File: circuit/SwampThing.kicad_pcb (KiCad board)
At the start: 2 copper layers, 102 parts, among them J1 USB_B, J2 HOLE, J3 HOLE, J4 HOLE, J5 HOLE, Q1 IRF530NPbF, Q2 BC547, SW1 reset, SW2 mute, SW3 HEAD/AD, SW4 vol+, SW5 vol-, SW6 next, SW7 prev, SW8 pause, U1 LM2576T-ADJ, U2 LM1117-5.0, U3 MAX6457, U4 LM1117-3.3, U5 TPA3220, U6 CSR_DBG, U7 CSR8645_MODULE

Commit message: SwampThing routed!
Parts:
- removed C13, C31: 470μF, NovaBox:CPOL_D10_P4.5
- removed C20: 10μF, NovaBox:CPOL_D6.3_P2.5
- removed C39: 1μF, NovaBox:CPOL_D4_P2
- removed S1: BATT_SEL, NovaBox:BATT_SEL
- removed SW4: vol+, NovaBox:Tact_6x6
- removed SW5: vol-, NovaBox:Tact_6x6
- removed SW7: prev, NovaBox:Tact_6x6
- added C6: 860μF, NovaBox:CPOL_D16_P7.5, F.Cu at (102.2, 80.6)
- added SW10: 4S LiPo, NovaBox:Switch_2.5mm, F.Cu at (77.9, 108.4)
- added SW11: 3S LiPo, NovaBox:Switch_2.5mm, F.Cu at (77.9, 105.9)
- added SW9: 6S LiPo, NovaBox:Switch_2.5mm, F.Cu at (77.9, 111.0)
- BT1: footprint NovaBox:XT60-M -> NovaBox:XT60PW-M
- C17, C19, C23, C24, C27, C34, C35: footprint NovaBox:C_5MM -> NovaBox:C_1206
- C38, C41: footprint NovaBox:CPOL_D4_P2 -> NovaBox:CPOL_D4_P1.27
- C4: value 100μF -> 860μF; footprint NovaBox:CPOL_D6.3_P2.5 -> NovaBox:CPOL_D16_P7.5
- C8: footprint NovaBox:CPOL_D10_P4.5 -> NovaBox:CPOL_D6.3_P2.5
- D5: value LED_RCBG -> LED_RABG; footprint NovaBox:LED_RCBG -> NovaBox:LED_RABG
- Q1: value IRF530NPbF -> IRF530NSPbF; footprint NovaBox:TO-220_Horizontal -> NovaBox:TO-252
- R11: value 1K -> 10K
- R24: value 470 -> 820
- R26: value 470 -> 220
- R27: value 470 -> 1K
- S2: value JUMPER_3WAY -> 18dB
- S3: value JUMPER_3WAY -> 24dB
- S4: value JUMPER_3WAY -> 30dB
- S5: value JUMPER_3WAY -> 34dB
- SW1, SW2: footprint NovaBox:Tact_6x6 -> NovaBox:Switch_2.5mm
- U1: footprint NovaBox:TO-220-5_Horizontal -> NovaBox:TO-263-5_TabPin3
- moved SW6 142.4 mm to (57.8, 52.1), turned to 90 degrees
- moved J1 127.1 mm to (47.6, 94.0), turned to 270 degrees
- moved J4 124.1 mm to (49.0, 34.0)
- moved C41 108.1 mm to (56.8, 95.9), turned to 270 degrees
- moved C5 107.2 mm to (130.8, 40.0)
- moved C10 106.5 mm to (105.4, 48.3)
- moved C12 106.0 mm to (102.3, 55.5)
- moved C15 106.0 mm to (130.8, 53.3)
- moved SPK1 105.9 mm to (140.4, 47.0)
- moved C11 105.6 mm to (105.4, 51.4)
- moved C29 105.6 mm to (105.4, 67.0)
- moved C30 105.6 mm to (106.1, 62.4)
- moved U5 105.6 mm to (96.0, 59.4)
- moved C22 105.6 mm to (106.1, 57.0)
- moved L2 105.6 mm to (118.1, 46.0)
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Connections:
- net +7V renamed +7.5V
- net Net-(C35-Pad1) renamed /GVDD
- net Net-(R20-Pad1) renamed /RESET
- C4 pad 1: +5V -> +BATT
- R11 pad 1: +5V -> +BATT
- R21 pad 1: Net-(R21-Pad1) -> GND
- R21 pad 2: GND -> /FREQ_ADJ
- R24 pad 2: Net-(D5-PadRA) -> Net-(D5-Pad1)
- R26 pad 2: Net-(D5-PadBA) -> Net-(D5-Pad3)
- R27 pad 2: Net-(D5-PadGA) -> Net-(D5-Pad4)
- U5 pad 14: Net-(R21-Pad1) -> /FREQ_ADJ
- U7 pad 30: /PREV -> (no net)
- U7 pad 32: /VOL- -> (no net)
- U7 pad 33: /VOL+ -> (no net)
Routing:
- net +BATT: track 0.00 -> 260.8 mm
- net +5V: track 0.00 -> 123.1 mm
- net GND: track 0.00 -> 85.6 mm, vias 0 -> 37
- net +7.5V: track 0.00 -> 58.7 mm, vias 0 -> 1
- net -BATT: track 0.00 -> 55.8 mm
- net +3V3: track 0.00 -> 55.3 mm, vias 0 -> 1
- net 1V8: track 0.00 -> 54.6 mm, vias 0 -> 1
- net Net-(S2-Pad2): track 0.00 -> 53.7 mm
- net VBUS: track 0.00 -> 47.5 mm, vias 0 -> 1
- net Net-(J1-Pad3): track 0.00 -> 43.6 mm, vias 0 -> 1
- net SPK_RP: track 0.00 -> 41.7 mm
- net Net-(J1-Pad2): track 0.00 -> 41.4 mm, vias 0 -> 1
- net SPK_RN: track 0.00 -> 41.0 mm
- net SPK_LP: track 0.00 -> 40.0 mm
- net SPK_LN: track 0.00 -> 39.4 mm
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- added copper zone on B.Cu, net GND
- added copper zone on F.Cu, net GND
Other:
- board outline added: 100 x 100 mm
- board text added: "AD"
- board text added: "HEAD"
- board text added: "SwampThing"

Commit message: PCB done
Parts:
- added REF**: OSHW-Symbol_44.5x40mm_SilkScreen, NovaBox:OSHW-Symbol_44.5x40mm_SilkScreen, B.Cu at (121.3, 58.4)
- added REF**: KiCad-Logo2_12mm_SilkScreen, NovaBox:KiCad-Logo2_12mm_SilkScreen, B.Cu at (125.7, 92.7)
- L1: footprint NovaBox:COIL_LHL10TB681K -> NovaBox:COILCRAFT_RFS1317
- moved D1 14.6 mm to (115.6, 106.0), turned to 180 degrees
- moved C2 5.68 mm to (102.9, 106.0), turned to 180 degrees
- moved R4 4.45 mm to (103.5, 116.2)
- moved R2 4.44 mm to (106.0, 116.2)
- moved L1 2.54 mm to (116.2, 116.2)
- moved SW2 1.80 mm to (88.9, 80.6), turned to 180 degrees
- moved R20 0.90 mm to (87.6, 53.3)
- moved BT1 0.63 mm to (47.6, 112.4)
- turned C21 to 0 degrees
- turned C6 to 180 degrees
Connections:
- J1 pad 5: Net-(J1-Pad5) -> (no net)
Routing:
- net +5V: track 123.1 -> 138.4 mm
- net Net-(R2-Pad2): track 20.8 -> 25.3 mm
- net Net-(D1-Pad1): track 26.4 -> 22.0 mm
- net +BATT: track 260.8 -> 257.6 mm
- net Net-(U6-Pad3): track 8.85 -> 11.1 mm
- net +3V3: track 55.3 -> 53.3 mm
- net +7.5V: track 58.7 -> 57.2 mm, vias 1 -> 0
- net HEAD: track 20.6 -> 19.2 mm
- net Net-(U6-Pad5): track 9.45 -> 10.5 mm
- net Net-(C38-Pad2): track 9.13 -> 9.83 mm
- net Net-(C19-Pad2): track 7.41 -> 8.05 mm
- net -BATT: track 55.8 -> 55.1 mm
- net Net-(U6-Pad7): track 10.6 -> 11.1 mm
- net Net-(R8-Pad1): track 12.3 -> 12.8 mm
- net /OUT2_M: track 26.4 -> 26.9 mm
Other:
- board text added: "Swamp thing"
- board text added: "by Ferenc Szili 2019.feb.24"
- board text added: "https://github.com/nodep/NovaBox"
- board text removed: "SwampThing"

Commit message: still have to check the electrolytics
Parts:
- C4, C6: value 860μF -> 1000μF
- R12, R17: value 470 -> 1K
- moved REF** 0.19 mm to (125.7, 92.9)
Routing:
- net /SW_GATE: track 27.0 -> 41.7 mm
- net -BATT: track 55.1 -> 57.1 mm
- net Net-(R10-Pad1): track 13.5 -> 12.7 mm
- net Net-(R8-Pad1): track 12.8 -> 12.1 mm
- net Net-(R9-Pad1): track 13.2 -> 12.7 mm

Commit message: i think this should be it
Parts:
- C1: footprint NovaBox:CPOL_D8_P3.5 -> NovaBox:CPOL_D10_P4.5
- C3: footprint NovaBox:CPOL_D6.3_P2.5 -> NovaBox:CPOL_D4_P1.5
- C38, C41: footprint NovaBox:CPOL_D4_P1.27 -> NovaBox:CPOL_D4_P1.5
- moved REF** 2.08 mm to (127.6, 92.1)
- moved C41 0.74 mm to (57.1, 96.5)
- moved C1 0.64 mm to (128.3, 104.1)
- moved D1 0.63 mm to (114.9, 106.0)
- moved C3 0.31 mm to (103.5, 94.6)
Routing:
- net VBUS: track 47.5 -> 48.1 mm

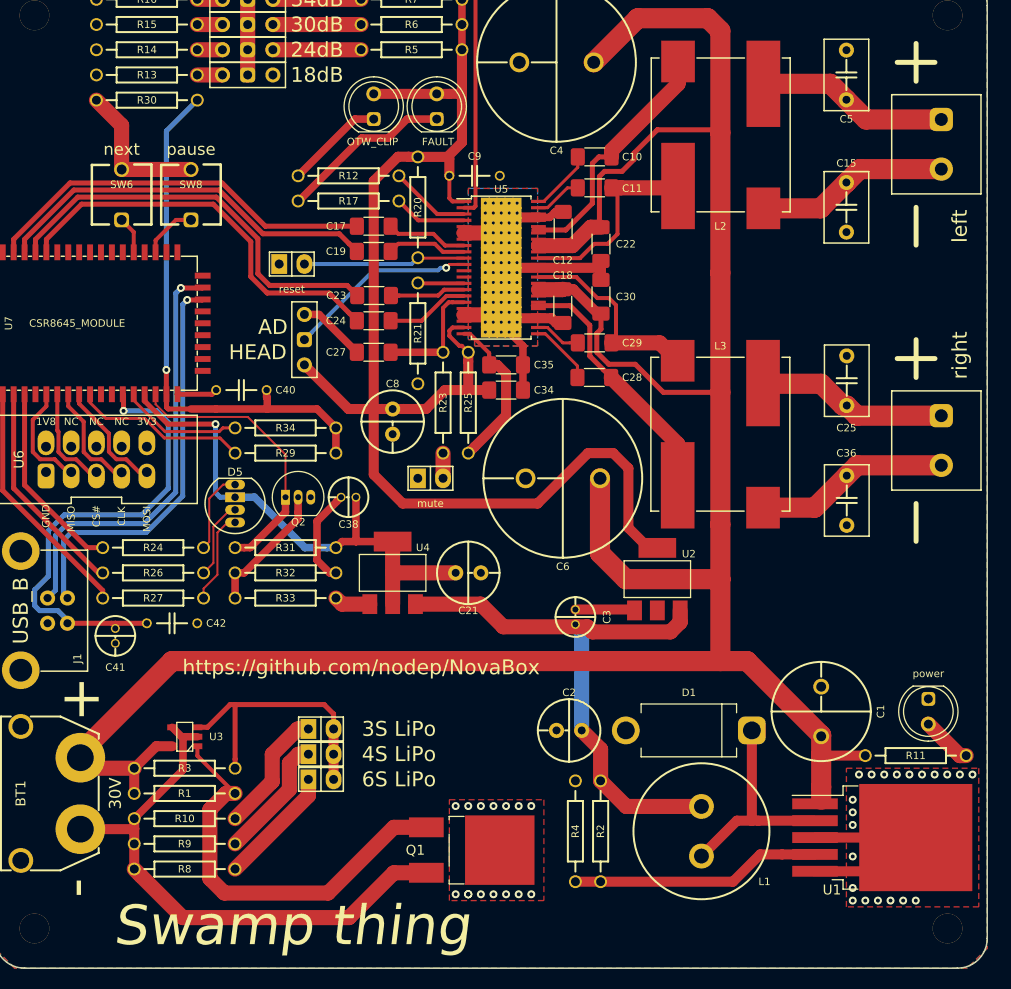
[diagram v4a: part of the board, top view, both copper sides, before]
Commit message: sent swamp thing to the fab fixed problem with voltages above 16V on the WhiteBoy
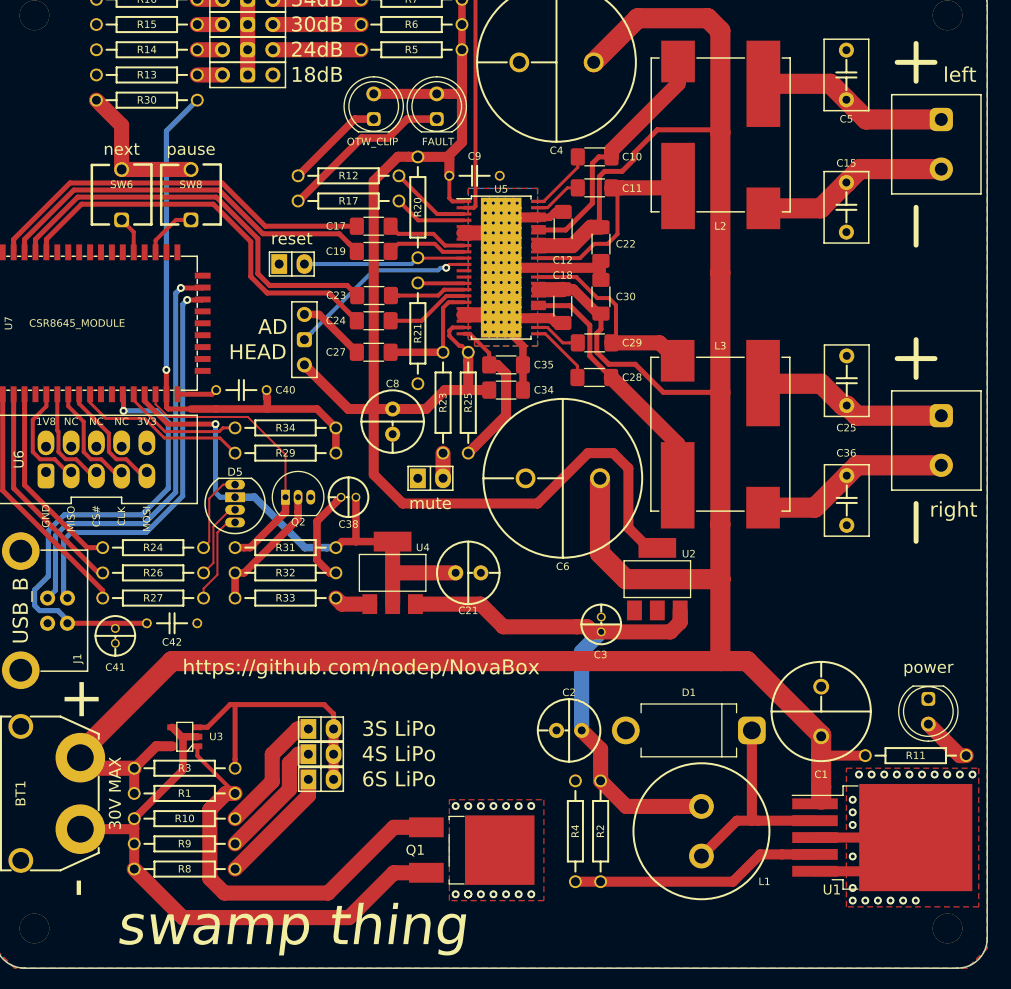
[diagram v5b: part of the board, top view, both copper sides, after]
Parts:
- BT1: value 30V -> 30V MAX
- moved C3 2.71 mm to (106.1, 95.4)
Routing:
- net GND: track 85.4 -> 79.4 mm
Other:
- board text added: "by Ferenc Szili 2019.feb.26"
- board text added: "swamp thing"
- board text removed: "Swamp thing"
- board text removed: "by Ferenc Szili 2019.feb.24"
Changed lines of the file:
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@@
     (thickness 1.6)
     (drawings 13)
-    (tracks 576)
+    (tracks 574)
     (zones 0)
     (modules 100)
@@
   )
   (setup
-    (last_trace_width 1.016)
+    (last_trace_width 0.2032)
     (user_trace_width 0.254)
     (user_trace_width 0.3048)
@@
     (add_net VBUS)
   )
+  (module NovaBox:SW_SPDT_JUMPER (layer F.Cu)
+    (at 76.2 66.675 90)
+    (fp_text reference SW3 (at -1.375 0.6 90) (layer F.SilkS) hide
+      (effects (font (size 0.0254 0.0254) (thickness 0.001)))
+    )
+    (fp_text value HEAD/AD (at 0 -0.5 90) (layer F.Fab) hide
+      (effects (font (size 0.0254 0.0254) (thickness 0.001)))
+    )
+    (fp_line (start -3.81 1.27) (end -3.81 -1.27) (layer F.SilkS) (width 0.15))
+    (fp_line (start 3.81 1.27) (end -3.81 1.27) (layer F.SilkS) (width 0.15))
+    (fp_line (start 3.81 -1.27) (end 3.81 1.27) (layer F.SilkS) (width 0.15))
+    (fp_line (start -3.81 -1.27) (end 3.81 -1.27) (layer F.SilkS) (width 0.15))
+    (pad 3 thru_hole circle (at 2.54 0 90) (size 1.524 1.524) (drill 0.9) (layers *.Cu *.Mask)
+      (net 3 GND))
+    (pad 2 thru_hole roundrect (at 0 0 90) (size 1.524 1.524) (drill 0.9) (layers *.Cu *.Mask) (roundrect_rratio 0.25)
+      (net 57 HEAD))
+    (pad 1 thru_hole circle (at -2.54 0 90) (size 1.524 1.524) (drill 0.9) (layers *.Cu *.Mask)
+      (net 4 +5V))
+    (model ${KISYS3DMOD}/Connector_PinHeader_2.54mm.3dshapes/PinHeader_1x03_P2.54mm_Vertical.wrl
+      (offset (xyz 2.54 0 0))
+      (scale (xyz 1 1 1))
+      (rotate (xyz 0 0 90))
+    )
+  )
   (module NovaBox:CPOL_D10_P4.5 (layer F.Cu)
     (at 128.27 104.14 90)
-    (fp_text reference C1 (at 0 6 90) (layer F.SilkS)
+    (fp_text reference C1 (at -6.35 0 180) (layer F.SilkS)
       (effects (font (size 0.75 0.75) (thickness 0.15)))
     )
@@
   )
   (module NovaBox:CPOL_D4_P1.5 (layer F.Cu)
-    (at 103.505 94.615 90)
-    (fp_text reference C3 (at 0 3.175 90) (layer F.SilkS)
+    (at 106.1085 95.365 90)
+    (fp_text reference C3 (at -3.06 -0.0635 180) (layer F.SilkS)
       (effects (font (size 0.75 0.75) (thickness 0.15)))
     )
@@
       (effects (font (size 0.0254 0.0254) (thickness 0.001)))
     )
-    (fp_text value power (at -3.81 0 180) (layer F.SilkS)
-      (effects (font (size 0.75 0.75) (thickness 0.15)))
+    (fp_text value power (at -4.445 0 180) (layer F.SilkS)
+      (effects (font (size 1.2 1.2) (thickness 0.2)))
     )
     (fp_line (start -2.56 -1.545) (end -2.56 1.545) (layer F.SilkS) (width 0.12))
@@
       (effects (font (size 0.127 0.127) (thickness 0.01524)))
     )
-    (fp_text value left (at -8.255 1.87 270) (layer F.SilkS)
+    (fp_text value left (at 6.985 1.87) (layer F.SilkS)
       (effects (font (size 1.5 1.5) (thickness 0.3)))
     )
@@
       (effects (font (size 0.127 0.127) (thickness 0.01524)))
     )
-    (fp_text value right (at 8.58 1.87 270) (layer F.SilkS)
+    (fp_text value right (at -6.985 1.235) (layer F.SilkS)
       (effects (font (size 1.5 1.5) (thickness 0.3)))
     )
@@
   (module NovaBox:C_5MM (layer F.Cu)
     (at 62.865 95.25 180)
-    (fp_text reference C42 (at -4.445 0) (layer F.SilkS)
+    (fp_text reference C42 (at 0 -1.905) (layer F.SilkS)
       (effects (font (size 0.75 0.75) (thickness 0.15)))
     )
@@
     )
   )
-  (module NovaBox:SW_SPDT_JUMPER (layer F.Cu)
-    (at 76.2 66.675 90)
-    (fp_text reference SW3 (at -1.375 0.6 90) (layer F.SilkS) hide
-      (effects (font (size 0.0254 0.0254) (thickness 0.001)))
-    )
-    (fp_text value HEAD/AD (at 0 -0.5 90) (layer F.Fab) hide
-      (effects (font (size 0.0254 0.0254) (thickness 0.001)))
-    )
-    (fp_line (start -3.81 -1.27) (end 3.81 -1.27) (layer F.SilkS) (width 0.15))
-    (fp_line (start 3.81 -1.27) (end 3.81 1.27) (layer F.SilkS) (width 0.15))
-    (fp_line (start 3.81 1.27) (end -3.81 1.27) (layer F.SilkS) (width 0.15))
-    (fp_line (start -3.81 1.27) (end -3.81 -1.27) (layer F.SilkS) (width 0.15))
-    (pad 1 thru_hole circle (at -2.54 0 90) (size 1.524 1.524) (drill 0.9) (layers *.Cu *.Mask)
-      (net 4 +5V))
-    (pad 2 thru_hole roundrect (at 0 0 90) (size 1.524 1.524) (drill 0.9) (layers *.Cu *.Mask) (roundrect_rratio 0.25)
-      (net 57 HEAD))
-    (pad 3 thru_hole circle (at 2.54 0 90) (size 1.524 1.524) (drill 0.9) (layers *.Cu *.Mask)
-      (net 3 GND))
-  )
   (module NovaBox:XT60PW-M (layer F.Cu)
     (at 47.625 112.395 90)
@@
       (effects (font (size 1 1) (thickness 0.15)))
     )
-    (fp_text value 30V (at 0 9.525 90) (layer F.SilkS)
+    (fp_text value "30V MAX" (at 0 9.525 90) (layer F.SilkS)
       (effects (font (size 1.2 1.2) (thickness 0.2)))
     )
@@
       (effects (font (size 0.127 0.127) (thickness 0.0254)))
     )
-    (fp_text value reset (at 0 -2.54 180) (layer F.SilkS)
-      (effects (font (size 0.75 0.75) (thickness 0.127)))
+    (fp_text value reset (at 0 2.54 180) (layer F.SilkS)
+      (effects (font (size 1.2 1.2) (thickness 0.2)))
     )
     (fp_line (start -2.254 1.2) (end -2.254 -1.2) (layer F.SilkS) (width 0.1524))
@@
     )
     (fp_text value mute (at 0 -2.54) (layer F.SilkS)
-      (effects (font (size 0.75 0.75) (thickness 0.127)))
+      (effects (font (size 1.2 1.2) (thickness 0.2)))
     )
     (fp_line (start 0 1.2) (end 0 -1.2) (layer F.SilkS) (width 0.1524))
@@
     (effects (font (size 1.5 1.5) (thickness 0.3)))
   )
-  (gr_text "by Ferenc Szili 2019.feb.24" (at 104.775 126.365) (layer B.SilkS)
+  (gr_text "by Ferenc Szili 2019.feb.26" (at 102.87 126.365) (layer B.SilkS)
     (effects (font (size 3 3) (thickness 0.5) italic) (justify mirror))
   )
-  (gr_text "Swamp thing" (at 74.93 125.73) (layer F.SilkS)
+  (gr_text "swamp thing" (at 74.93 125.73) (layer F.SilkS)
     (effects (font (size 4 4) (thickness 0.6) italic))
   )
@@
   (via (at 97.79 113.665) (size 0.8) (drill 0.4) (layers F.Cu B.Cu) (net 3))
   (via (at 99.06 113.665) (size 0.8) (drill 0.4) (layers F.Cu B.Cu) (net 3))
-  (segment (start 109.37 93.865) (end 109.46 93.955) (width 1.016) (layer F.Cu) (net 3))
-  (segment (start 103.505 93.865) (end 109.37 93.865) (width 1.016) (layer F.Cu) (net 3))
   (via (at 134.62 110.49) (size 0.8) (drill 0.4) (layers F.Cu B.Cu) (net 3))
   (segment (start 91.1236 65.4475) (end 90.805 65.7661) (width 0.4064) (layer F.Cu) (net 4))
@@
   (segment (start 106.045 107.95) (end 104.14 106.045) (width 1.524) (layer F.Cu) (net 74))
   (segment (start 106.045 111.125) (end 106.045 107.95) (width 1.524) (layer F.Cu) (net 74))
-  (segment (start 104.14 96.1136) (end 103.632 95.6056) (width 1.524) (layer B.Cu) (net 74))
-  (segment (start 104.14 106.045) (end 104.14 96.1136) (width 1.524) (layer B.Cu) (net 74))
   (segment (start 96.2406 95.6056) (end 103.632 95.6056) (width 1.524) (layer F.Cu) (net 74))
   (segment (start 87.39 93.32) (end 93.955 93.32) (width 1.524) (layer F.Cu) (net 74))
@@
   (segment (start 103.632 95.6056) (end 104.70963 95.6056) (width 1.524) (layer F.Cu) (net 74))
   (segment (start 104.70963 95.6056) (end 105.222398 96.118368) (width 1.524) (layer F.Cu) (net 74))
+  (segment (start 104.14 98.0835) (end 106.1085 96.115) (width 1.524) (layer B.Cu) (net 74))
+  (segment (start 104.14 106.045) (end 104.14 98.0835) (width 1.524) (layer B.Cu) (net 74))
   (zone (net 3) (net_name GND) (layer B.Cu) (hatch edge 0.508)
     (connect_pads yes (clearance 0.254))

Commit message: changed the MAX6457 voltage divider values new calcVoltage
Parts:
- Q1: value IRF530NSPbF -> IRFS52N15DTRLP
- R10: value 90K9 -> 2.26M
- R3: value 750K -> 16.9M
- R8: value 115K -> 1.05M
- R9: value 90K9 -> 1.62M
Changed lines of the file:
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@@
       (effects (font (size 1 1) (thickness 0.15)))
     )
-    (fp_text value IRF530NSPbF (at -1.905 0.635) (layer F.Fab)
+    (fp_text value IRFS52N15DTRLP (at -1.905 0.635) (layer F.Fab)
       (effects (font (size 0.05 0.05) (thickness 0.01)))
     )
@@
       (effects (font (size 0.75 0.75) (thickness 0.15)))
     )
-    (fp_text value 750K (at -2.286 0) (layer F.Fab) hide
+    (fp_text value 16.9M (at -2.286 0) (layer F.Fab) hide
       (effects (font (size 0.127 0.127) (thickness 0.001)))
     )
@@
       (effects (font (size 0.75 0.75) (thickness 0.15)))
     )
-    (fp_text value 115K (at -2.286 0 180) (layer F.Fab) hide
+    (fp_text value 1.05M (at -2.286 0 180) (layer F.Fab) hide
       (effects (font (size 0.127 0.127) (thickness 0.001)))
     )
@@
       (effects (font (size 0.75 0.75) (thickness 0.15)))
     )
-    (fp_text value 90K9 (at -2.286 0 180) (layer F.Fab) hide
+    (fp_text value 1.62M (at -2.286 0 180) (layer F.Fab) hide
       (effects (font (size 0.127 0.127) (thickness 0.001)))
     )
@@
       (effects (font (size 0.75 0.75) (thickness 0.15)))
     )
-    (fp_text value 90K9 (at -2.286 0 180) (layer F.Fab) hide
-      (effects (font (size 0.127 0.127) (thickness 0.001)))
-    )
+    (fp_text value 2.26M (at -2.286 0 180) (layer F.Fab) hide
+      (effects (font (size 0.127 0.127) (thickness 0.001)))
+    )
